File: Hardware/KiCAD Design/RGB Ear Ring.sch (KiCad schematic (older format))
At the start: 11 parts, among them J1 AVR-ISP-6, U1 ATtiny85V-10MU

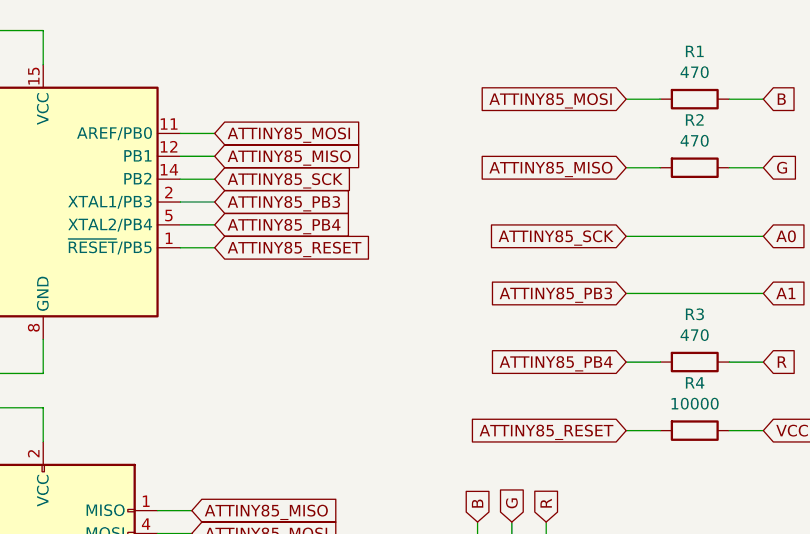
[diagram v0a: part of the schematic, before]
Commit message: Posted 1051 - (V2.1)
Hardware Update for newer version.  Allows for PWM function on Blue pins.
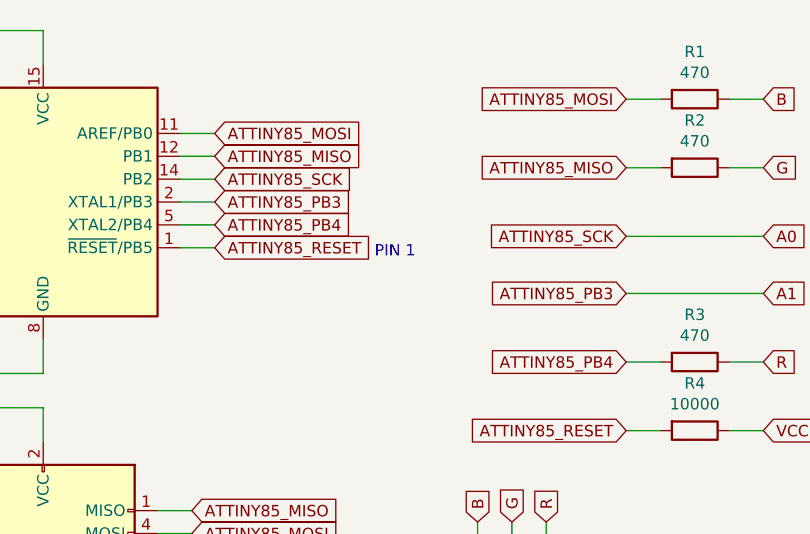
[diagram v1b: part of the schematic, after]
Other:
- note added: "PIN 1"
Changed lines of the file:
@@
 Wire Wire Line
 	4450 2200 4600 2200
+Text Notes 3350 1750 0    50   ~ 0
+PIN 1
 $EndSCHEMATC
